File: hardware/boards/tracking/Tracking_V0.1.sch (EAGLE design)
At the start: 37 parts, among them J1 CON_HEADER_PRG_AVR_ICSP-PTH, U1 ATMEGA328P-AU, U3 USD-SOCKETNEW

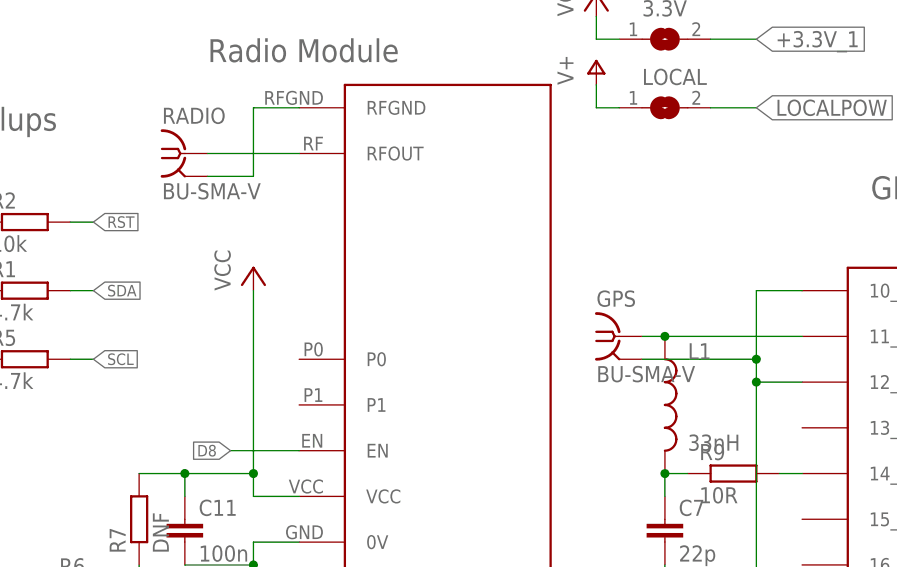
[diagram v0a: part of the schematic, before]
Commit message: Switched to right angle SMA connectors, created 3d render
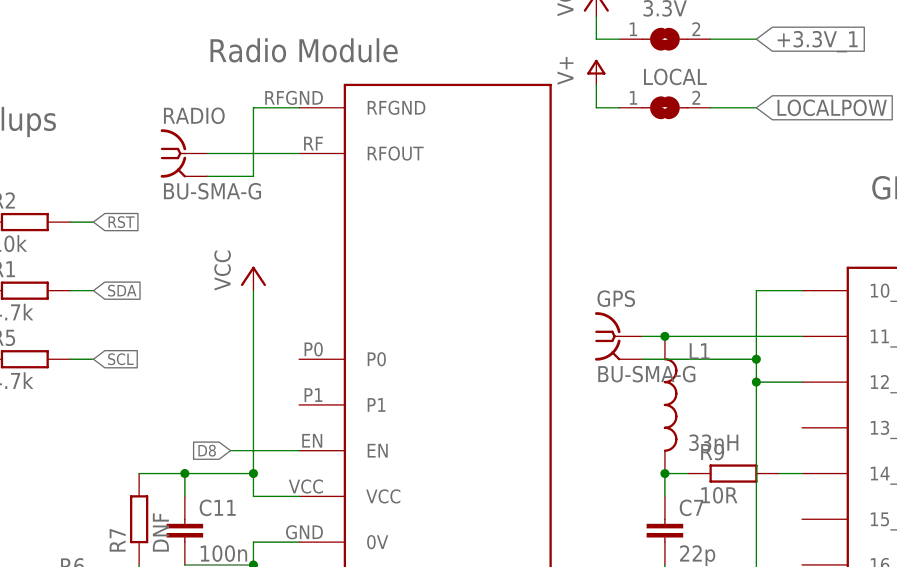
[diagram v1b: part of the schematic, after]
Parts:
- GPS, RADIO: value BU-SMA-V -> BU-SMA-G; device con-coax:BU-SMA-V -> con-coax:BU-SMA-G; OC_FARNELL 2144531 -> (none)
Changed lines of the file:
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@@
 <part name="GND9" library="supply1" deviceset="GND" device=""/>
 <part name="P+4" library="supply1" deviceset="VCC" device=""/>
-<part name="GPS" library="con-coax" deviceset="BU-SMA-V" device="">
-<attribute name="OC_FARNELL" value="2144531"/>
-</part>
 <part name="C12" library="rcl" deviceset="C-EU" device="C0603" value="100n">
 <attribute name="OC_FARNELL" value="2429362"/>
@@
 <part name="GND11" library="supply1" deviceset="GND" device=""/>
 <part name="3V6" library="supply1" deviceset="VCC" device=""/>
-<part name="RADIO" library="con-coax" deviceset="BU-SMA-V" device="">
-<attribute name="OC_FARNELL" value="2144531"/>
-</part>
 <part name="U$6" library="Ava" deviceset="RADIOMETRIX-MTX2" device=""/>
 <part name="C11" library="rcl" deviceset="C-EU" device="C0603" value="100n">
@@
 <part name="P+5" library="supply1" deviceset="V+" device=""/>
 <part name="JP1" library="pinhead" deviceset="PINHD-2X11" device=""/>
+<part name="GPS" library="con-coax" deviceset="BU-SMA-G" device=""/>
+<part name="RADIO" library="con-coax" deviceset="BU-SMA-G" device=""/>
 </parts>
 <sheets>
@@
 <instance part="GND9" gate="1" x="83.82" y="0"/>
 <instance part="P+4" gate="VCC" x="137.16" y="55.88"/>
-<instance part="GPS" gate="G$1" x="68.58" y="43.18"/>
 <instance part="C12" gate="G$1" x="142.24" y="33.02">
 <attribute name="OC_FARNELL" x="142.24" y="33.02" size="1.27" layer="96" display="off"/>
@@
 <instance part="GND11" gate="1" x="27.94" y="-2.54"/>
 <instance part="3V6" gate="VCC" x="27.94" y="50.8"/>
-<instance part="RADIO" gate="G$1" x="20.32" y="63.5"/>
 <instance part="U$6" gate="G$1" x="48.26" y="40.64" rot="R270"/>
 <instance part="C11" gate="G$1" x="20.32" y="22.86">
@@
 <instance part="P+5" gate="1" x="66.04" y="73.66"/>
 <instance part="JP1" gate="A" x="289.56" y="12.7"/>
+<instance part="GPS" gate="G1" x="68.58" y="43.18"/>
+<instance part="RADIO" gate="G1" x="20.32" y="63.5"/>
 </instances>
 <busses>
@@
 <wire x1="88.9" y1="38.1" x2="83.82" y2="38.1" width="0.1524" layer="91"/>
 <junction x="83.82" y="38.1"/>
-<pinref part="GPS" gate="G$1" pin="2"/>
 <wire x1="71.12" y1="40.64" x2="83.82" y2="40.64" width="0.1524" layer="91"/>
 <junction x="83.82" y="40.64"/>
@@
 <wire x1="73.66" y1="15.24" x2="83.82" y2="15.24" width="0.1524" layer="91"/>
 <junction x="83.82" y="15.24"/>
+<pinref part="GPS" gate="G1" pin="2"/>
 </segment>
 <segment>
@@
 <segment>
 <pinref part="U$4" gate="G$1" pin="11_RF_IN"/>
-<pinref part="GPS" gate="G$1" pin="1"/>
 <wire x1="88.9" y1="43.18" x2="73.66" y2="43.18" width="0.1524" layer="91"/>
 <pinref part="L1" gate="G$1" pin="1"/>
 <wire x1="73.66" y1="43.18" x2="71.12" y2="43.18" width="0.1524" layer="91"/>
 <junction x="73.66" y="43.18"/>
+<pinref part="GPS" gate="G1" pin="1"/>
 </segment>
 </net>
@@
 <net name="RFGND" class="0">
 <segment>
-<pinref part="RADIO" gate="G$1" pin="2"/>
 <wire x1="22.86" y1="60.96" x2="27.94" y2="60.96" width="0.1524" layer="91"/>
 <wire x1="33.02" y1="68.58" x2="27.94" y2="68.58" width="0.1524" layer="91"/>
 <wire x1="27.94" y1="68.58" x2="27.94" y2="60.96" width="0.1524" layer="91"/>
 <pinref part="U$6" gate="G$1" pin="RFGND"/>
+<pinref part="RADIO" gate="G1" pin="2"/>
 </segment>
 </net>
 <net name="N$6" class="0">
 <segment>
-<pinref part="RADIO" gate="G$1" pin="1"/>
 <wire x1="33.02" y1="63.5" x2="22.86" y2="63.5" width="0.1524" layer="91"/>
 <pinref part="U$6" gate="G$1" pin="RFOUT"/>
-</segment>
-</net>
+<pinref part="RADIO" gate="G1" pin="1"/>
+</segment>
+</net>
